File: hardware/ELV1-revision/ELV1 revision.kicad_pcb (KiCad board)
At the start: 2 copper layers, 115 x 85.1 mm, 228 parts, among them J1 15VAC 30VA Transformer out, J10 PROGRAM PINS, J2 FAN1, J3 FAN2, J4 Conn_02x10_Odd_Even, J5 DS18B20, J6 power in (outside), J7 power in (outside), Q1 IRLML6344TRPBF, Q2 IRLML6344TRPBF, Q3 IRLML6344TRPBF, Q4 IRLML6344TRPBF, Q5 IRLML6344TRPBF, Q6 IRLML6344TRPBF, SW3 SW_Push, U10 IRFB4110PBF, U12 SRV05-4, U13 LTV-817S, U15 CH340G, U16 SY6280AAC, U17 TPS54302, U2 MCP4725xxx-xCH, U20 STM32G071CBT6, U21 ADS1115IDGS, U3 AP2112K-3.3, U4 OPA2197xD, U6 TPS54302, U7 IRFP260NPBF, U8 IRFP260NPBF, U9 ADS1115IDGS, Y1 12MHZ CRYSTAL, Y2 ABM7-8.000MHZ-D2Y-T

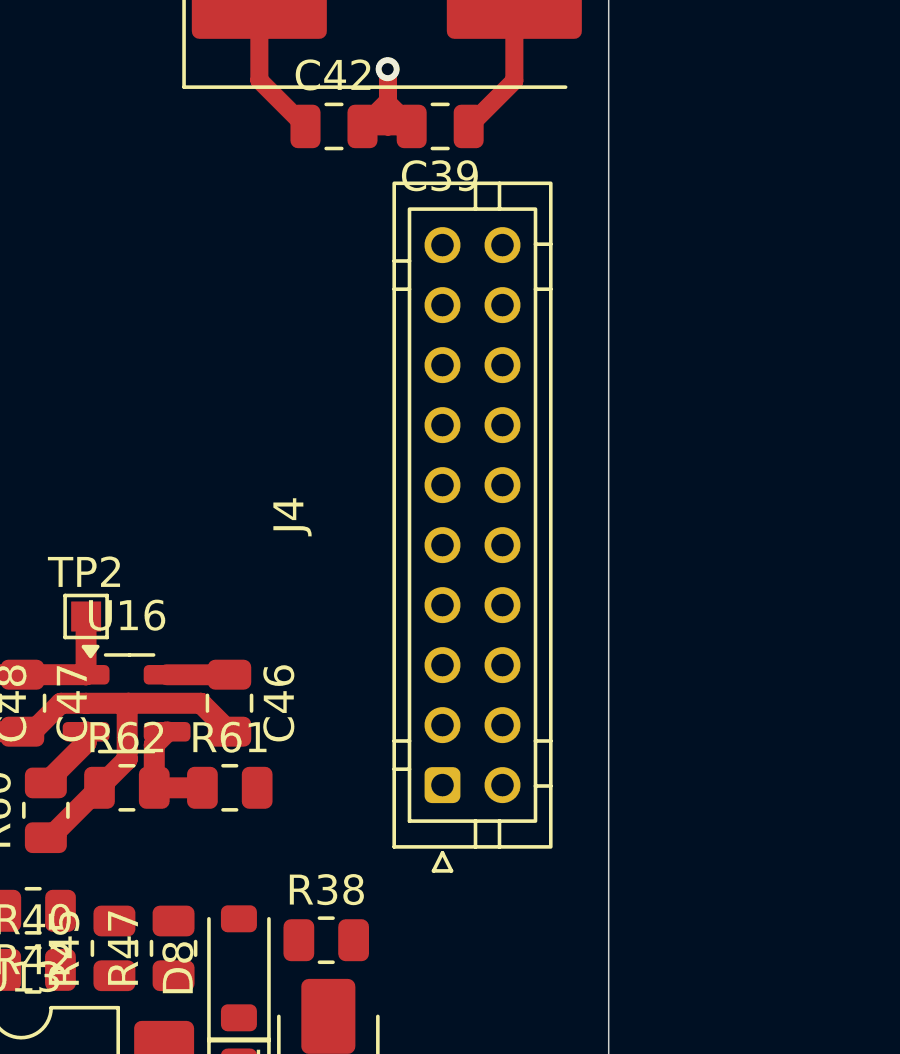
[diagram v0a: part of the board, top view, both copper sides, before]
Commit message: Revert J4 footprint change (connector stays KLS PHB 2.0); note ELV1 temporary X-cap bleeder
This reverts commit 97f4282.

Co-Authored-By: Claude Opus 5.5 <noreply@anthropic.com>
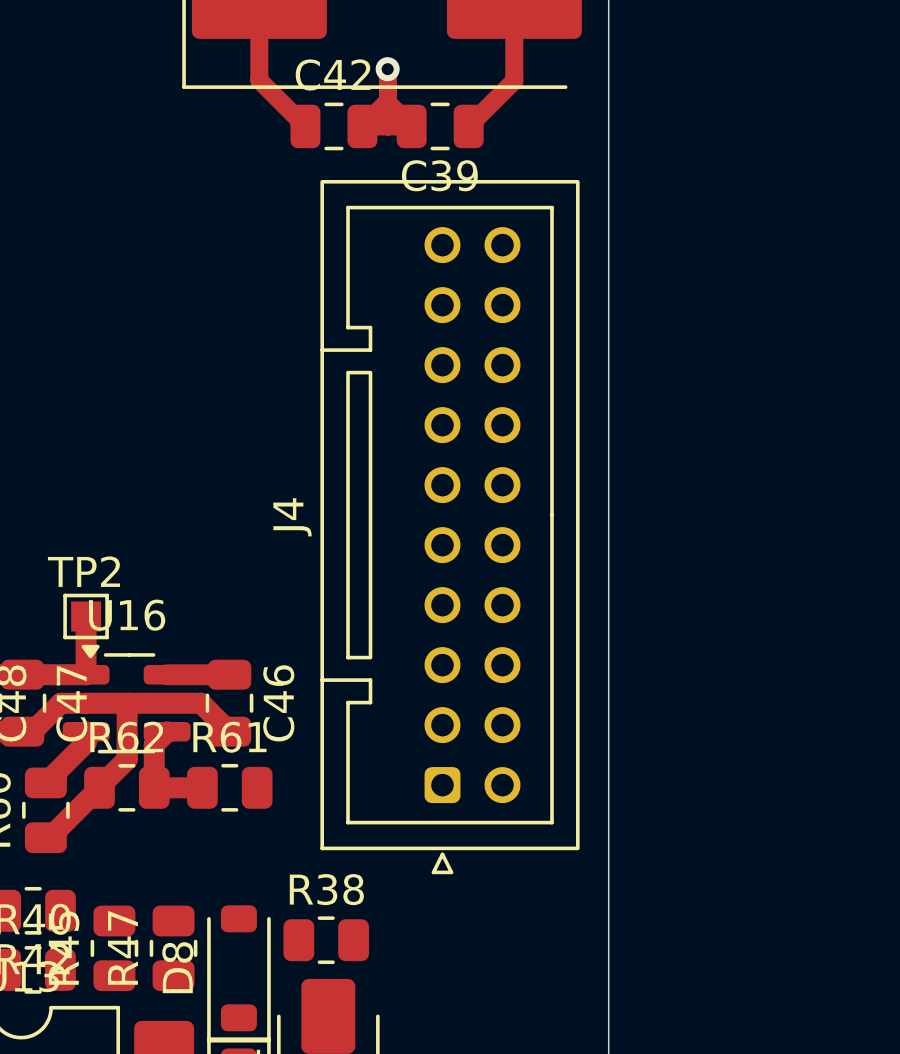
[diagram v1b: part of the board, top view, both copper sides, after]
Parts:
- J4: footprint Connector_JST:JST_PHD_B20B-PHDSS_2x10_P2.00mm_Vertical -> Connector_JST:JST_PUD_B20B-PUDSS_2x10_P2.00mm_Vertical

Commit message: ELV1 revision: J4 footprint JST PUD -> JST PHD (B20B-PHDSS), same pad grid
Co-Authored-By: Claude Opus 5.5 <noreply@anthropic.com>
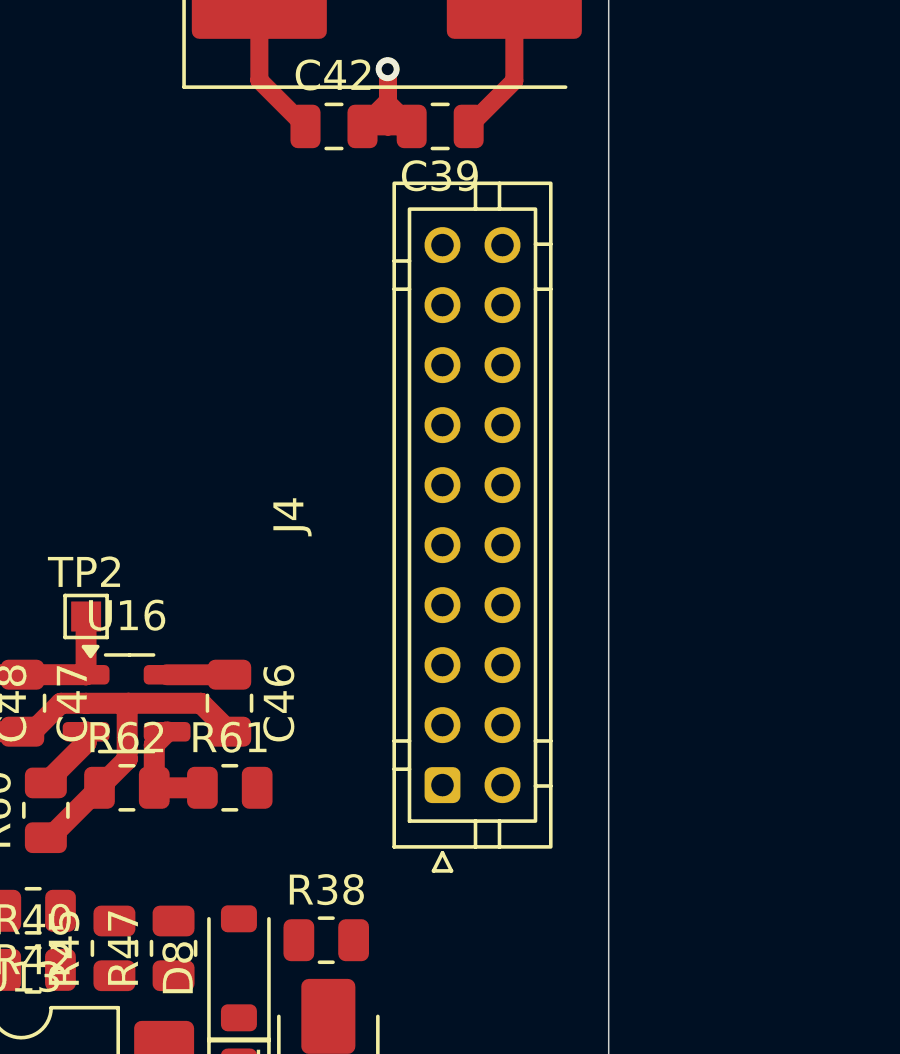
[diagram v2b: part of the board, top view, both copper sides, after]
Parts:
- J4: footprint Connector_JST:JST_PUD_B20B-PUDSS_2x10_P2.00mm_Vertical -> Connector_JST:JST_PHD_B20B-PHDSS_2x10_P2.00mm_Vertical
